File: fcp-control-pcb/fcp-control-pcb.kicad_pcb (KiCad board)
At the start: 2 copper layers, 151.1 x 137.2 mm, 215 parts, among them IC1 L01Z050S05, J1 Conn_01x15_Female, J10 LittlePump, J11 BigPump, J12 OUT0, J13 Conn_01x10_Male, J14 Conn_01x10_Male, J15 Conn_01x10_Male, J2 Conn_01x15_Female, J3 CAPACITOR, J4 FUELCELL, J6 DISCHARGER, J7 CHARGER, J8 LimiterBypass, J9 Current_Mode, Q1 AONR21321, Q2 Q_NMOS_GDS, Q3 Q_NMOS_GDS, Q4 Q_NMOS_GDS, U1 MAX15462AB, U10 LM2902, U11 LM2902, U12 LM2902, U13 CD74HC4067SM, U14 CD74HC4067SM, U2 LM311DR, U3 TLI4971-A050T5-U-E0001, U5 LM2902, U6 LM2902, U7 LM2902, U8 LM2902, U9 LM2902

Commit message: adds vias to fcc fuse
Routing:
- net VCC: track 80.2 -> 80.5 mm, vias 2 -> 10
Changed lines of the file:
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@@
   (segment (start 188.595 100.33) (end 193.675 100.33) (width 3) (layer "F.Cu") (net 29))
   (segment (start 181.51 107.415) (end 188.595 100.33) (width 3) (layer "F.Cu") (net 29))
-  (segment (start 198.755 95.25) (end 198.755 72.39) (width 3) (layer "F.Cu") (net 29))
   (segment (start 114.935 116.205) (end 118.745 120.015) (width 1) (layer "F.Cu") (net 29))
   (segment (start 181.51 126.365) (end 181.51 117.475) (width 3) (layer "F.Cu") (net 29))
@@
   (segment (start 181.51 108.585) (end 181.51 117.475) (width 3) (layer "F.Cu") (net 29))
   (segment (start 124.2275 109.22) (end 124.2275 107.0825) (width 1) (layer "F.Cu") (net 29))
+  (segment (start 198.755 95.25) (end 198.755 73.025) (width 3) (layer "F.Cu") (net 29))
   (segment (start 124.2275 109.22) (end 124.2275 110.2575) (width 1) (layer "F.Cu") (net 29))
   (segment (start 193.675 100.33) (end 198.755 95.25) (width 3) (layer "F.Cu") (net 29))
+  (segment (start 198.755 73.025) (end 198.12 72.39) (width 3) (layer "F.Cu") (net 29))
   (segment (start 124.2275 110.2575) (end 127 113.03) (width 1) (layer "F.Cu") (net 29))
+  (via (at 199.39 72.39) (size 0.8) (drill 0.4) (layers "F.Cu" "B.Cu") (free) (net 29))
+  (via (at 193.04 67.31) (size 0.8) (drill 0.4) (layers "F.Cu" "B.Cu") (free) (net 29))
+  (via (at 193.04 72.39) (size 0.8) (drill 0.4) (layers "F.Cu" "B.Cu") (free) (net 29))
   (via (at 118.745 120.015) (size 0.8) (drill 0.4) (layers "F.Cu" "B.Cu") (net 29))
+  (via (at 199.39 67.31) (size 0.8) (drill 0.4) (layers "F.Cu" "B.Cu") (free) (net 29))
+  (via (at 195.58 72.39) (size 0.8) (drill 0.4) (layers "F.Cu" "B.Cu") (free) (net 29))
   (via (at 122.555 105.41) (size 0.8) (drill 0.4) (layers "F.Cu" "B.Cu") (net 29))
+  (via (at 199.39 69.85) (size 0.8) (drill 0.4) (layers "F.Cu" "B.Cu") (free) (net 29))
+  (via (at 195.58 69.85) (size 0.8) (drill 0.4) (layers "F.Cu" "B.Cu") (free) (net 29))
+  (via (at 195.58 67.31) (size 0.8) (drill 0.4) (layers "F.Cu" "B.Cu") (free) (net 29))
   (segment (start 124.8625 114.935) (end 128.11 114.935) (width 0.6) (layer "F.Cu") (net 30))
   (segment (start 124.2275 114.3) (end 124.8625 114.935) (width 0.6) (layer "F.Cu") (net 30))

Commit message: layout changes
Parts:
- moved H2 56.8 mm to (190.5, 83.8)
- moved H4 32.1 mm to (88.9, 147.3)
- moved H1 13.5 mm to (191.8, 147.3)
- moved H3 1.27 mm to (58.4, 29.2)
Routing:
- net VCC: track 80.5 -> 74.7 mm, vias 10 -> 7
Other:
- board size 151.1 x 137.2 mm -> 144.8 x 128.3 mm
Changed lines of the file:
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@@
   )
   (footprint "MountingHole:MountingHole_3.2mm_M3" (layer "F.Cu")
-    (at 200.66 27.94)
+    (at 190.5 83.82)
     (descr "Mounting Hole 3.2mm, no annular, M3")
     (tags "mounting hole 3.2mm no annular m3")
@@
       (effects (font (size 1 1) (thickness 0.15)))
     )
-    (fp_text user "${REFERENCE}" (at 0 0) (layer "F.Fab")
-      (effects (font (size 1 1) (thickness 0.15)))
-    )
     (fp_circle (center 0 0) (end 3.2 0) (layer "Cmts.User") (width 0.15) (fill none))
     (fp_circle (center 0 0) (end 3.45 0) (layer "F.CrtYd") (width 0.05) (fill none))
@@
   )
   (footprint "MountingHole:MountingHole_3.2mm_M3" (layer "F.Cu")
-    (at 200.66 157.48)
+    (at 191.77 147.32)
     (descr "Mounting Hole 3.2mm, no annular, M3")
     (tags "mounting hole 3.2mm no annular m3")
@@
   )
   (footprint "MountingHole:MountingHole_3.2mm_M3" (layer "F.Cu")
-    (at 58.42 157.48)
+    (at 88.9 147.32)
     (descr "Mounting Hole 3.2mm, no annular, M3")
     (tags "mounting hole 3.2mm no annular m3")
@@
   )
   (footprint "MountingHole:MountingHole_3.2mm_M3" (layer "F.Cu")
-    (at 58.42 27.94)
+    (at 58.42 29.21)
     (descr "Mounting Hole 3.2mm, no annular, M3")
     (tags "mounting hole 3.2mm no annular m3")
@@
     )
   )
-  (gr_rect (start 53.34 24.13) (end 204.47 161.29) (layer "Edge.Cuts") (width 0.1) (fill none))
+  (gr_rect (start 53.34 25.4) (end 198.12 153.67) (layer "Edge.Cuts") (width 0.1) (fill none))
   (gr_text "+ FuelCell -" (at 142.24 46.99) (layer "F.SilkS")
     (effects (font (size 1 1) (thickness 0.15)))
@@
   (segment (start 106.716956 53.34) (end 109.22 53.34) (width 1) (layer "B.Cu") (net 27))
   (segment (start 135.9 67.31) (end 140.98 67.31) (width 1) (layer "B.Cu") (net 28))
-  (segment (start 188.595 100.33) (end 193.675 100.33) (width 3) (layer "F.Cu") (net 29))
-  (segment (start 181.51 107.415) (end 188.595 100.33) (width 3) (layer "F.Cu") (net 29))
+  (segment (start 181.51 108.585) (end 181.51 105.51) (width 3) (layer "F.Cu") (net 29))
   (segment (start 114.935 116.205) (end 118.745 120.015) (width 1) (layer "F.Cu") (net 29))
   (segment (start 181.51 126.365) (end 181.51 117.475) (width 3) (layer "F.Cu") (net 29))
+  (segment (start 181.51 105.51) (end 193.04 93.98) (width 3) (layer "F.Cu") (net 29))
   (segment (start 124.2275 107.0825) (end 122.555 105.41) (width 1) (layer "F.Cu") (net 29))
+  (segment (start 193.04 93.98) (end 195.58 91.44) (width 3) (layer "F.Cu") (net 29))
   (segment (start 127 113.03) (end 128.27 113.03) (width 1) (layer "F.Cu") (net 29))
-  (segment (start 181.51 108.585) (end 181.51 107.415) (width 3) (layer "F.Cu") (net 29))
   (segment (start 181.51 108.585) (end 181.51 117.475) (width 3) (layer "F.Cu") (net 29))
   (segment (start 124.2275 109.22) (end 124.2275 107.0825) (width 1) (layer "F.Cu") (net 29))
-  (segment (start 198.755 95.25) (end 198.755 73.025) (width 3) (layer "F.Cu") (net 29))
   (segment (start 124.2275 109.22) (end 124.2275 110.2575) (width 1) (layer "F.Cu") (net 29))
-  (segment (start 193.675 100.33) (end 198.755 95.25) (width 3) (layer "F.Cu") (net 29))
-  (segment (start 198.755 73.025) (end 198.12 72.39) (width 3) (layer "F.Cu") (net 29))
+  (segment (start 195.58 91.44) (end 195.58 73.66) (width 3) (layer "F.Cu") (net 29))
   (segment (start 124.2275 110.2575) (end 127 113.03) (width 1) (layer "F.Cu") (net 29))
-  (via (at 199.39 72.39) (size 0.8) (drill 0.4) (layers "F.Cu" "B.Cu") (free) (net 29))
   (via (at 193.04 67.31) (size 0.8) (drill 0.4) (layers "F.Cu" "B.Cu") (free) (net 29))
   (via (at 193.04 72.39) (size 0.8) (drill 0.4) (layers "F.Cu" "B.Cu") (free) (net 29))
   (via (at 118.745 120.015) (size 0.8) (drill 0.4) (layers "F.Cu" "B.Cu") (net 29))
-  (via (at 199.39 67.31) (size 0.8) (drill 0.4) (layers "F.Cu" "B.Cu") (free) (net 29))
   (via (at 195.58 72.39) (size 0.8) (drill 0.4) (layers "F.Cu" "B.Cu") (free) (net 29))
   (via (at 122.555 105.41) (size 0.8) (drill 0.4) (layers "F.Cu" "B.Cu") (net 29))
-  (via (at 199.39 69.85) (size 0.8) (drill 0.4) (layers "F.Cu" "B.Cu") (free) (net 29))
   (via (at 195.58 69.85) (size 0.8) (drill 0.4) (layers "F.Cu" "B.Cu") (free) (net 29))
   (via (at 195.58 67.31) (size 0.8) (drill 0.4) (layers "F.Cu" "B.Cu") (free) (net 29))
@@
     (polygon
       (pts
-        (xy 201.93 74.93)
+        (xy 198.12 74.93)
         (xy 187.96 74.93)
         (xy 187.96 64.77)
-        (xy 201.93 64.77)
+        (xy 198.12 64.77)
       )
     )
@@
     (polygon
       (pts
-        (xy 204.47 161.29)
-        (xy 53.34 161.29)
-        (xy 53.34 24.13)
-        (xy 204.47 24.13)
+        (xy 198.12 153.67)
+        (xy 53.34 153.67)
+        (xy 53.34 25.4)
+        (xy 198.12 25.4)
       )
     )
@@
     (polygon
       (pts
-        (xy 204.47 161.29)
-        (xy 93.345 161.29)
-        (xy 93.345 24.13)
-        (xy 204.47 24.13)
+        (xy 198.12 153.67)
+        (xy 93.345 153.67)
+        (xy 93.345 25.4)
+        (xy 198.12 25.4)
       )
     )
@@
     (polygon
       (pts
-        (xy 96.52 161.29)
-        (xy 53.34 161.29)
-        (xy 53.34 24.13)
-        (xy 96.52 24.13)
+        (xy 96.52 153.67)
+        (xy 53.34 153.67)
+        (xy 53.34 25.4)
+        (xy 96.52 25.4)
       )
     )

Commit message: silscreen
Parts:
- added G***: LOGO, LOGO, F.Cu at (162.6, 142.2)
- added G***: LOGO, LOGO, F.Cu at (180.3, 133.3)
- added G***: LOGO, LOGO, B.Cu at (149.7, 113.5)
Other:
- board text added: "FCP Control 2.0"
- board text added: "Jesslyn"
- board text added: "Michelle"
- board text added: "Roy"
- board text added: "SEMA 2023"
- board text added: "Zavary"

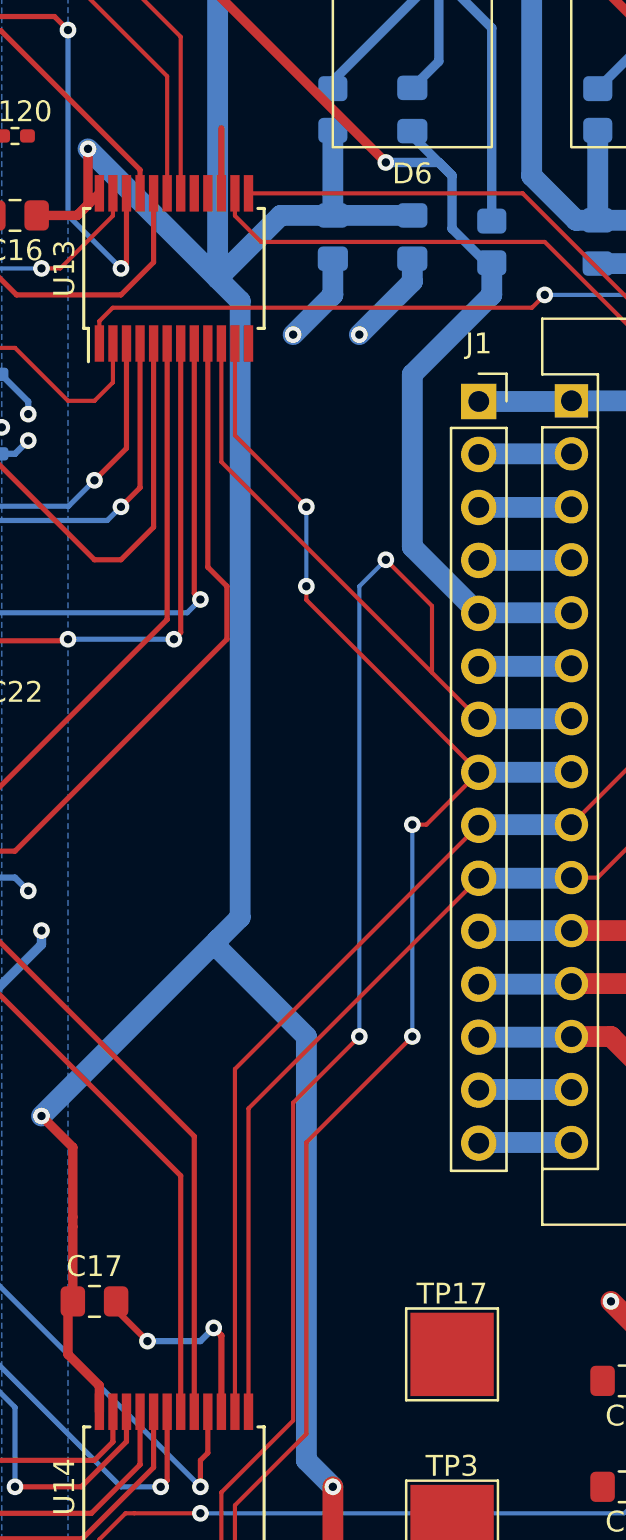
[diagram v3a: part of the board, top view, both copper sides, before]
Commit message: adds enable pin control to multiplexers
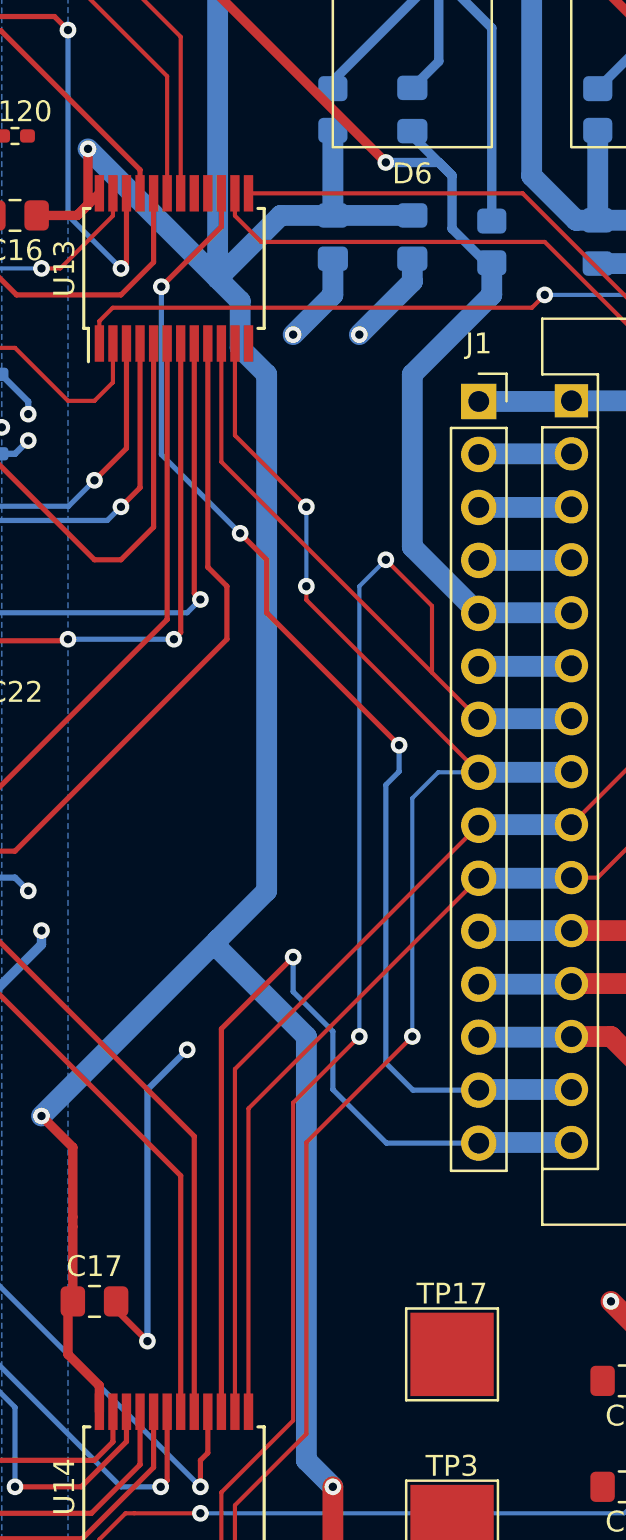
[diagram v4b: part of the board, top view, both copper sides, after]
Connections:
- U13 pad 15: GND -> /MOSI
- U14 pad 15: GND -> /MISO
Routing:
- net /MOSI: track 4.46 -> 57.3 mm, vias 0 -> 3
- net /MISO: track 4.46 -> 42.9 mm, vias 0 -> 1
- net GND: track 202.4 -> 206.4 mm
- net +5V: track 370.8 -> 371.9 mm
- net /D5: track 73.0 -> 73.7 mm, vias 4 -> 3
